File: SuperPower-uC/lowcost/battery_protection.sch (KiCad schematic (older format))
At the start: 7 parts, among them J1 Battery connector, J7 DNP, U1 AP9101CK6-ADTRG1, U2 FS8205A

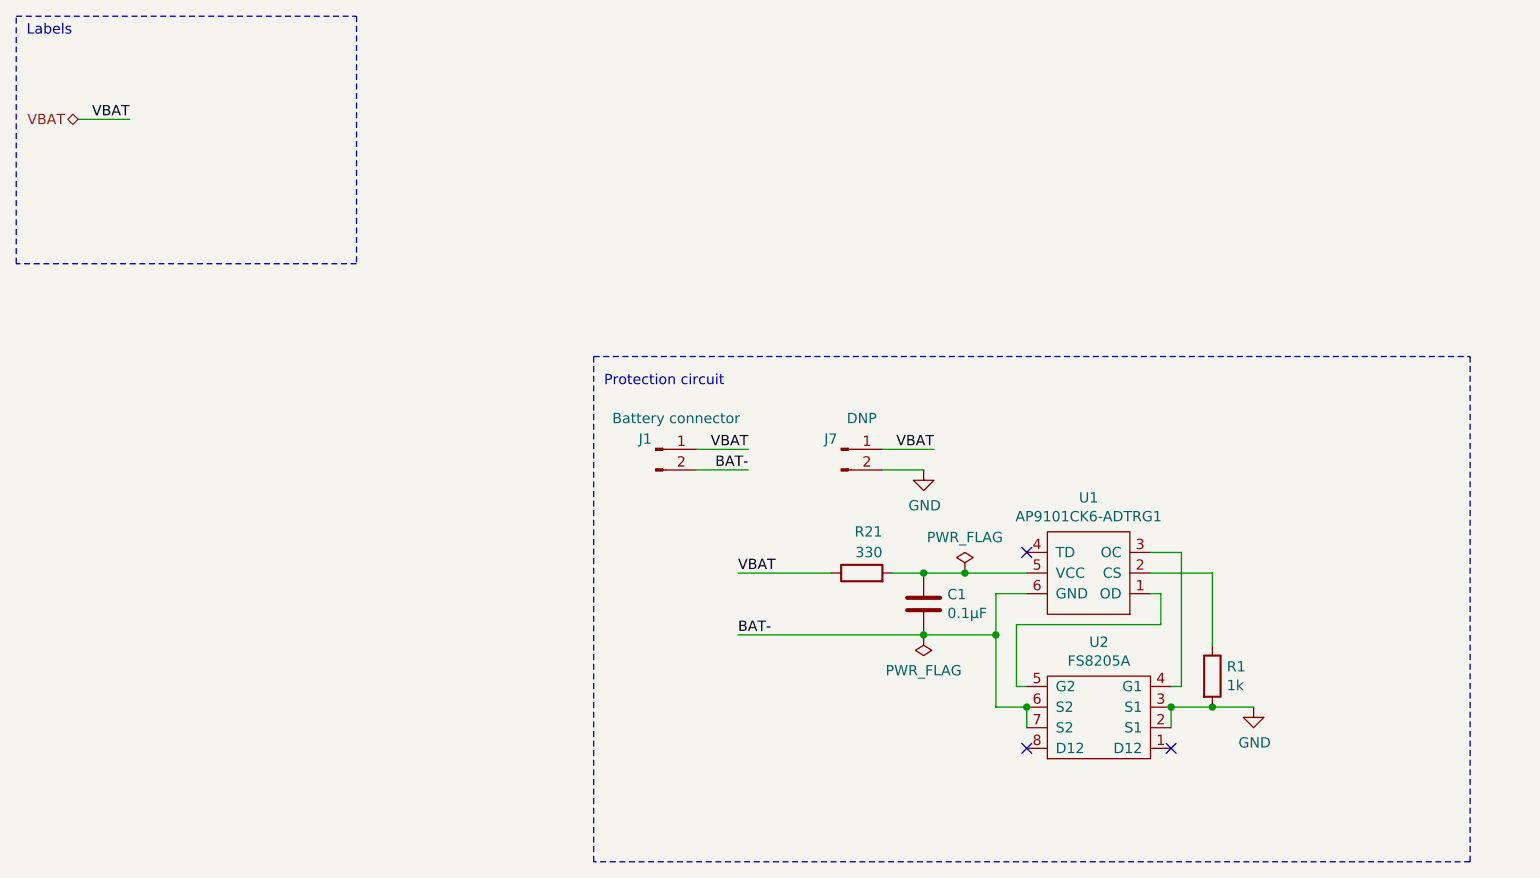
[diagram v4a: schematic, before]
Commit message: comments and optimisation
added some comments to the schematic swapped the CHARGE_DISABLE pin for another GND pin
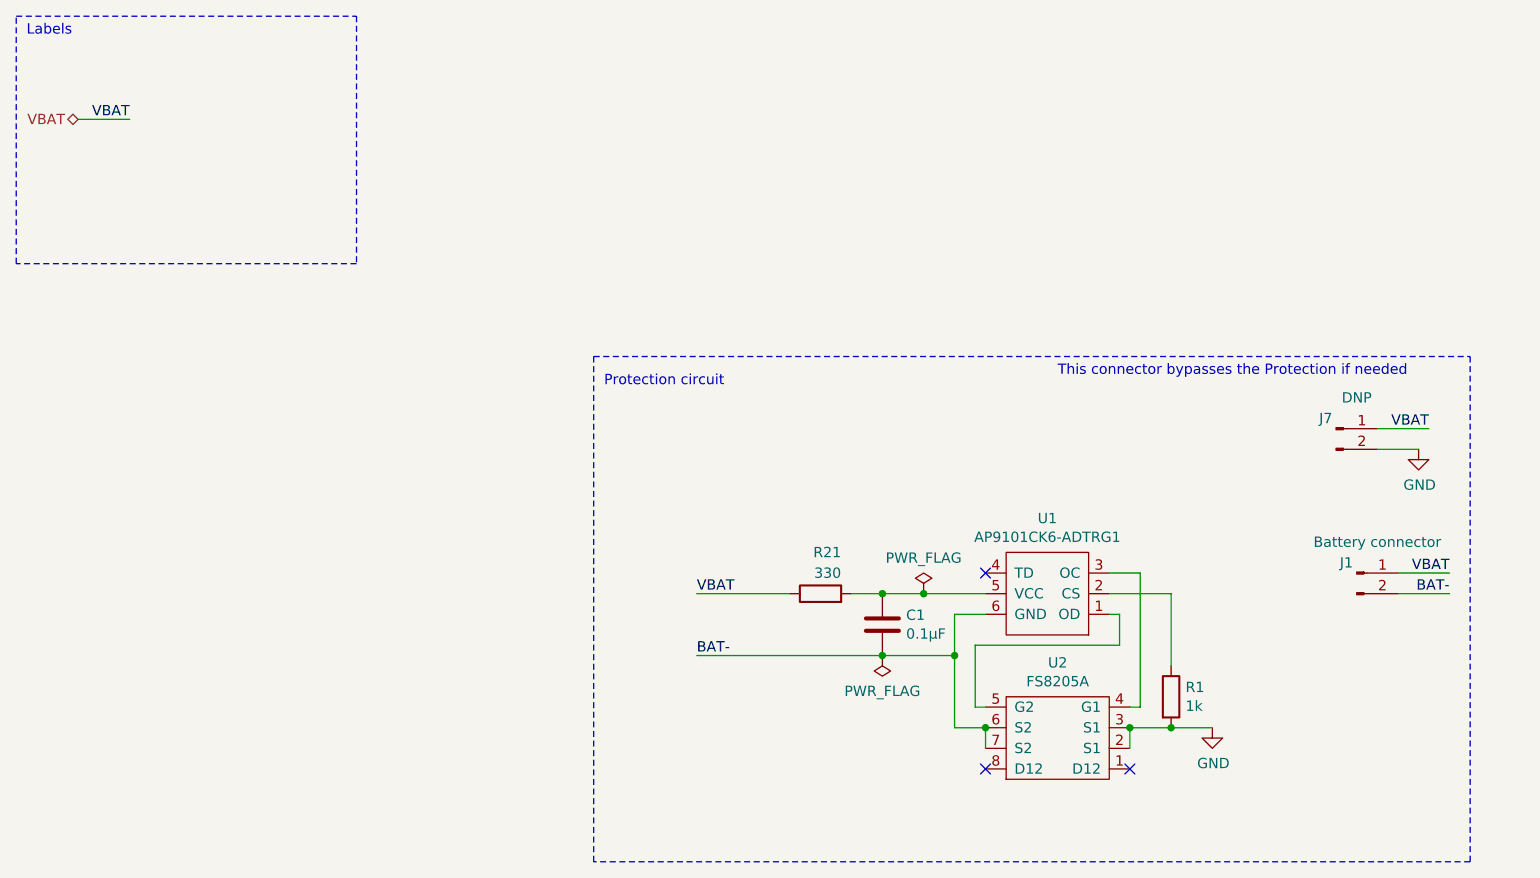
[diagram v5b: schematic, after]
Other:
- note added: "This connector bypasses the Protection if needed"
- moved on the sheet: C1, J1, J7, R1, R21, U1, U2
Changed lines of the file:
@@
 L FS312F-G:FS312F-G U1
 U 1 1 5F7C508D
-P 5750 3350
-F 0 "U1" H 5750 2885 50  0000 C CNN
-F 1 "AP9101CK6-ADTRG1" H 5750 2976 50  0000 C CNN
-F 2 "Package_TO_SOT_SMD:SOT-23-6_Handsoldering" H 5850 3800 50  0001 C CNN
-F 3 "https://www.diodes.com/assets/Datasheets/AP9101C.pdf" H 5750 3100 50  0001 C CNN
-F 4 "C151339" H 5750 3350 50  0001 C CNN "LCSC"
-	1    5750 3350
+P 5550 3450
+F 0 "U1" H 5550 2985 50  0000 C CNN
+F 1 "AP9101CK6-ADTRG1" H 5550 3076 50  0000 C CNN
+F 2 "Package_TO_SOT_SMD:SOT-23-6_Handsoldering" H 5650 3900 50  0001 C CNN
+F 3 "https://www.diodes.com/assets/Datasheets/AP9101C.pdf" H 5550 3200 50  0001 C CNN
+F 4 "C151339" H 5550 3450 50  0001 C CNN "LCSC"
+	1    5550 3450
 	-1   0    0    1
 $EndComp
@@
 L FS8205A:FS8205A U2
 U 1 1 5F7C57B0
-P 5800 4000
-F 0 "U2" H 5800 3585 50  0000 C CNN
-F 1 "FS8205A" H 5800 3676 50  0000 C CNN
-F 2 "Package_SO:TSSOP-8_4.4x3mm_P0.65mm" H 5800 4300 50  0001 C CNN
-F 3 "https://www.ic-fortune.com/upload/Download/FS8205A-DS-12_EN.pdf" H 5800 4300 50  0001 C CNN
-F 4 "C16052" H 5800 4000 50  0001 C CNN "LCSC"
-	1    5800 4000
+P 5600 4100
+F 0 "U2" H 5600 3685 50  0000 C CNN
+F 1 "FS8205A" H 5600 3776 50  0000 C CNN
+F 2 "Package_SO:TSSOP-8_4.4x3mm_P0.65mm" H 5600 4400 50  0001 C CNN
+F 3 "https://www.ic-fortune.com/upload/Download/FS8205A-DS-12_EN.pdf" H 5600 4400 50  0001 C CNN
+F 4 "C16052" H 5600 4100 50  0001 C CNN "LCSC"
+	1    5600 4100
 	-1   0    0    1
 $EndComp
 Wire Wire Line
-	5450 3800 5400 3800
-Wire Wire Line
-	5400 3800 5400 3500
-Wire Wire Line
-	5400 3500 6100 3500
-Wire Wire Line
-	6100 3500 6100 3350
-Wire Wire Line
-	6100 3350 6050 3350
-Wire Wire Line
-	6050 3150 6200 3150
-Wire Wire Line
-	6200 3150 6200 3800
-Wire Wire Line
-	6200 3800 6150 3800
-Wire Wire Line
-	5450 4000 5450 3900
-Wire Wire Line
-	5450 3900 5300 3900
-Wire Wire Line
-	5300 3350 5450 3350
-Connection ~ 5450 3900
-Wire Wire Line
-	5450 3250 5150 3250
-Wire Wire Line
-	5300 3550 4950 3550
+	5250 3900 5200 3900
+Wire Wire Line
+	5200 3900 5200 3600
+Wire Wire Line
+	5200 3600 5900 3600
+Wire Wire Line
+	5900 3600 5900 3450
+Wire Wire Line
+	5900 3450 5850 3450
+Wire Wire Line
+	5850 3250 6000 3250
+Wire Wire Line
+	6000 3250 6000 3900
+Wire Wire Line
+	6000 3900 5950 3900
+Wire Wire Line
+	5250 4100 5250 4000
+Wire Wire Line
+	5250 4000 5100 4000
+Wire Wire Line
+	5100 3450 5250 3450
+Connection ~ 5250 4000
+Wire Wire Line
+	5250 3350 4950 3350
+Wire Wire Line
+	5100 3650 4750 3650
 $Comp
 L Device:R R1
 U 1 1 5F7CFA8D
-P 6350 3750
-F 0 "R1" H 6420 3796 50  0000 L CNN
-F 1 "1k" H 6420 3705 50  0000 L CNN
-F 2 "Resistor_SMD:R_0603_1608Metric_Pad1.05x0.95mm_HandSolder" V 6280 3750 50  0001 C CNN
-F 3 "~" H 6350 3750 50  0001 C CNN
-F 4 "C21190" H 6350 3750 50  0001 C CNN "LCSC"
-	1    6350 3750
+P 6150 3850
+F 0 "R1" H 6220 3896 50  0000 L CNN
+F 1 "1k" H 6220 3805 50  0000 L CNN
+F 2 "Resistor_SMD:R_0603_1608Metric_Pad1.05x0.95mm_HandSolder" V 6080 3850 50  0001 C CNN
+F 3 "~" H 6150 3850 50  0001 C CNN
+F 4 "C21190" H 6150 3850 50  0001 C CNN "LCSC"
+	1    6150 3850
 	1    0    0    -1
 $EndComp
@@
 L Device:C C1
 U 1 1 5F7D0298
-P 4950 3400
-F 0 "C1" H 5065 3446 50  0000 L CNN
-F 1 "0.1µF" H 5065 3355 50  0000 L CNN
-F 2 "Capacitor_SMD:C_0603_1608Metric_Pad1.05x0.95mm_HandSolder" H 4988 3250 50  0001 C CNN
-F 3 "~" H 4950 3400 50  0001 C CNN
-F 4 "C14858" H 4950 3400 50  0001 C CNN "LCSC"
-	1    4950 3400
-	1    0    0    -1
-$EndComp
-Connection ~ 4950 3550
-Connection ~ 5300 3550
-Wire Wire Line
-	5300 3550 5300 3350
-Wire Wire Line
-	5300 3550 5300 3900
-Wire Wire Line
-	6150 4000 6150 3900
-Connection ~ 6150 3900
-Wire Wire Line
-	6350 3600 6350 3250
-Wire Wire Line
-	6350 3250 6050 3250
+P 4750 3500
+F 0 "C1" H 4865 3546 50  0000 L CNN
+F 1 "0.1µF" H 4865 3455 50  0000 L CNN
+F 2 "Capacitor_SMD:C_0603_1608Metric_Pad1.05x0.95mm_HandSolder" H 4788 3350 50  0001 C CNN
+F 3 "~" H 4750 3500 50  0001 C CNN
+F 4 "C14858" H 4750 3500 50  0001 C CNN "LCSC"
+	1    4750 3500
+	1    0    0    -1
+$EndComp
+Connection ~ 4750 3650
+Connection ~ 5100 3650
+Wire Wire Line
+	5100 3650 5100 3450
+Wire Wire Line
+	5100 3650 5100 4000
+Wire Wire Line
+	5950 4100 5950 4000
+Connection ~ 5950 4000
+Wire Wire Line
+	6150 3700 6150 3350
+Wire Wire Line
+	6150 3350 5850 3350
 $Comp
 L power:GND #PWR0101
 U 1 1 5F7D3A76
-P 6550 3900
-F 0 "#PWR0101" H 6550 3650 50  0001 C CNN
-F 1 "GND" H 6555 3727 50  0000 C CNN
-F 2 "" H 6550 3900 50  0001 C CNN
-F 3 "" H 6550 3900 50  0001 C CNN
-	1    6550 3900
-	1    0    0    -1
-$EndComp
-Connection ~ 6350 3900
+P 6350 4000
+F 0 "#PWR0101" H 6350 3750 50  0001 C CNN
+F 1 "GND" H 6355 3827 50  0000 C CNN
+F 2 "" H 6350 4000 50  0001 C CNN
+F 3 "" H 6350 4000 50  0001 C CNN
+	1    6350 4000
+	1    0    0    -1
+$EndComp
+Connection ~ 6150 4000
 $Comp
 L Connector:Conn_01x02_Male J1
 U 1 1 5F7D5382
-P 3650 2650
-F 0 "J1" H 3600 2700 50  0000 C CNN
-F 1 "Battery connector" H 3750 2800 50  0000 C CNN
-F 2 "Connector_JST:JST_PH_S2B-PH-K_1x02_P2.00mm_Horizontal" H 3650 2650 50  0001 C CNN
-F 3 "https://datasheet.lcsc.com/szlcsc/1811051822_JST-Sales-America-S2B-XH-A-LF-SN_C157931.pdf" H 3650 2650 50  0001 C CNN
-F 4 "C157931" H 3650 2650 50  0001 C CNN "LCSC"
-	1    3650 2650
-	1    0    0    -1
-$EndComp
-NoConn ~ 5450 4100
-NoConn ~ 6150 4100
-NoConn ~ 5450 3150
-Wire Wire Line
-	6550 3900 6350 3900
+P 7050 3250
+F 0 "J1" H 7000 3300 50  0000 C CNN
+F 1 "Battery connector" H 7150 3400 50  0000 C CNN
+F 2 "Connector_JST:JST_PH_S2B-PH-K_1x02_P2.00mm_Horizontal" H 7050 3250 50  0001 C CNN
+F 3 "https://datasheet.lcsc.com/szlcsc/1811051822_JST-Sales-America-S2B-XH-A-LF-SN_C157931.pdf" H 7050 3250 50  0001 C CNN
+F 4 "C157931" H 7050 3250 50  0001 C CNN "LCSC"
+	1    7050 3250
+	1    0    0    -1
+$EndComp
+NoConn ~ 5250 4200
+NoConn ~ 5950 4200
+NoConn ~ 5250 3250
+Wire Wire Line
+	6350 4000 6150 4000
 $Comp
 L power:PWR_FLAG #FLG0102
 U 1 1 5F858ADE
-P 4950 3550
-F 0 "#FLG0102" H 4950 3625 50  0001 C CNN
-F 1 "PWR_FLAG" H 4950 3723 50  0000 C CNN
-F 2 "" H 4950 3550 50  0001 C CNN
-F 3 "~" H 4950 3550 50  0001 C CNN
-	1    4950 3550
+P 4750 3650
+F 0 "#FLG0102" H 4750 3725 50  0001 C CNN
+F 1 "PWR_FLAG" H 4750 3823 50  0000 C CNN
+F 2 "" H 4750 3650 50  0001 C CNN
+F 3 "~" H 4750 3650 50  0001 C CNN
+	1    4750 3650
 	-1   0    0    1
 $EndComp
@@
 Text HLabel 850  1050 0    50   BiDi ~ 0
 VBAT
-Text Label 4100 2650 2    50   ~ 0
-VBAT
-Wire Wire Line
-	4100 2650 3850 2650
+Text Label 7500 3250 2    50   ~ 0
+VBAT
+Wire Wire Line
+	7500 3250 7250 3250
 Text Label 1100 1050 2    50   ~ 0
 VBAT
@@
 L Device:R R21
 U 1 1 5F88C76A
-P 4650 3250
-F 0 "R21" V 4850 3150 50  0000 L CNN
-F 1 "330" V 4750 3150 50  0000 L CNN
-F 2 "Resistor_SMD:R_0603_1608Metric_Pad1.05x0.95mm_HandSolder" V 4580 3250 50  0001 C CNN
-F 3 "~" H 4650 3250 50  0001 C CNN
-F 4 "C23138" H 4650 3250 50  0001 C CNN "LCSC"
-	1    4650 3250
+P 4450 3350
+F 0 "R21" V 4650 3250 50  0000 L CNN
+F 1 "330" V 4550 3250 50  0000 L CNN
+F 2 "Resistor_SMD:R_0603_1608Metric_Pad1.05x0.95mm_HandSolder" V 4380 3350 50  0001 C CNN
+F 3 "~" H 4450 3350 50  0001 C CNN
+F 4 "C23138" H 4450 3350 50  0001 C CNN "LCSC"
+	1    4450 3350
 	0    -1   -1   0
 $EndComp
 Wire Wire Line
-	4800 3250 4950 3250
-Connection ~ 4950 3250
+	4600 3350 4750 3350
+Connection ~ 4750 3350
 $Comp
 L power:PWR_FLAG #FLG0101
 U 1 1 5F9839DC
-P 5150 3250
-F 0 "#FLG0101" H 5150 3325 50  0001 C CNN
-F 1 "PWR_FLAG" H 5150 3423 50  0000 C CNN
-F 2 "" H 5150 3250 50  0001 C CNN
-F 3 "~" H 5150 3250 50  0001 C CNN
-	1    5150 3250
-	1    0    0    -1
-$EndComp
-Connection ~ 5150 3250
-Wire Wire Line
-	5150 3250 4950 3250
-Text Label 4050 3250 0    50   ~ 0
-VBAT
-Wire Wire Line
-	4050 3250 4500 3250
-Text Label 5000 2650 2    50   ~ 0
-VBAT
-Wire Wire Line
-	5000 2650 4750 2650
-Text Label 4100 2750 2    50   ~ 0
+P 4950 3350
+F 0 "#FLG0101" H 4950 3425 50  0001 C CNN
+F 1 "PWR_FLAG" H 4950 3523 50  0000 C CNN
+F 2 "" H 4950 3350 50  0001 C CNN
+F 3 "~" H 4950 3350 50  0001 C CNN
+	1    4950 3350
+	1    0    0    -1
+$EndComp
+Connection ~ 4950 3350
+Wire Wire Line
+	4950 3350 4750 3350
+Text Label 3850 3350 0    50   ~ 0
+VBAT
+Wire Wire Line
+	3850 3350 4300 3350
+Text Label 7400 2550 2    50   ~ 0
+VBAT
+Wire Wire Line
+	7400 2550 7150 2550
+Text Label 7500 3350 2    50   ~ 0
 BAT-
 Wire Wire Line
-	3850 2750 4100 2750
-Text Label 4050 3550 0    50   ~ 0
+	7250 3350 7500 3350
+Text Label 3850 3650 0    50   ~ 0
 BAT-
 Wire Wire Line
-	4050 3550 4950 3550
-Wire Wire Line
-	6350 3900 6150 3900
+	3850 3650 4750 3650
+Wire Wire Line
+	6150 4000 5950 4000
 $Comp
 L Connector:Conn_01x02_Male J7
 U 1 1 60035EFF
-P 4550 2650
-F 0 "J7" H 4500 2700 50  0000 C CNN
-F 1 "DNP" H 4650 2800 50  0000 C CNN
-F 2 "Connector_JST:JST_PH_S2B-PH-K_1x02_P2.00mm_Horizontal" H 4550 2650 50  0001 C CNN
-F 3 "" H 4550 2650 50  0001 C CNN
-F 4 "" H 4550 2650 50  0001 C CNN "LCSC"
-	1    4550 2650
+P 6950 2550
+F 0 "J7" H 6900 2600 50  0000 C CNN
+F 1 "DNP" H 7050 2700 50  0000 C CNN
+F 2 "Connector_JST:JST_PH_S2B-PH-K_1x02_P2.00mm_Horizontal" H 6950 2550 50  0001 C CNN
+F 3 "" H 6950 2550 50  0001 C CNN
+F 4 "" H 6950 2550 50  0001 C CNN "LCSC"
+	1    6950 2550
 	1    0    0    -1
 $EndComp
@@
 L power:GND #PWR0129
 U 1 1 60037B5A
-P 4950 2750
-F 0 "#PWR0129" H 4950 2500 50  0001 C CNN
-F 1 "GND" H 4955 2577 50  0000 C CNN
-F 2 "" H 4950 2750 50  0001 C CNN
-F 3 "" H 4950 2750 50  0001 C CNN
-	1    4950 2750
-	1    0    0    -1
-$EndComp
-Wire Wire Line
-	4950 2750 4750 2750
+P 7350 2650
+F 0 "#PWR0129" H 7350 2400 50  0001 C CNN
+F 1 "GND" H 7355 2477 50  0000 C CNN
+F 2 "" H 7350 2650 50  0001 C CNN
+F 3 "" H 7350 2650 50  0001 C CNN
+	1    7350 2650
+	1    0    0    -1
+$EndComp
+Wire Wire Line
+	7350 2650 7150 2650
+Text Notes 5600 2300 0    50   ~ 0
+This connector bypasses the Protection if needed
 $EndSCHEMATC

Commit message: corrected part numbers and datasheets
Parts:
- J1: LCSC C157931 -> C157932
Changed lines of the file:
@@
 F 1 "Battery connector" H 7150 3400 50  0000 C CNN
 F 2 "Connector_JST:JST_PH_S2B-PH-K_1x02_P2.00mm_Horizontal" H 7050 3250 50  0001 C CNN
-F 3 "https://datasheet.lcsc.com/szlcsc/1811051822_JST-Sales-America-S2B-XH-A-LF-SN_C157931.pdf" H 7050 3250 50  0001 C CNN
-F 4 "C157931" H 7050 3250 50  0001 C CNN "LCSC"
+F 3 "https://datasheet.lcsc.com/szlcsc/1810261120_JST-Sales-America-S2B-PH-K-S-GW_C157932.pdf" H 7050 3250 50  0001 C CNN
+F 4 "C157932" H 7050 3250 50  0001 C CNN "LCSC"
 	1    7050 3250
 	1    0    0    -1
